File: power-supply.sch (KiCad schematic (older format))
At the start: 99 parts, among them IC1 TPS54561, J12 S2B-PH-K-S_LF__SN_, Q1 IRLML6402TRPBF, Q10 2N7002, Q11 2N7002, Q2 IRLML6402TRPBF, Q3 IRLML6402TRPBF, Q4 IRLML6402TRPBF, Q5 IRLML6402TRPBF, Q6 IRLML6402TRPBF, Q7 2N7002, Q8 2N7002, Q9 2N7002, U10 TPS62823DLCT, U11 TPS62823DLCT, U12 TPS62823DLCT, U13 TPS62823DLCT, U15 SN74LVC1G08DCKR, U16 SN74LS08DBR, U9 LM3881MME_NOPB

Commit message: Swapped PHY, P-MOSFETs fix
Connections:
- wire segments 349 -> 355
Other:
- moved on the sheet: C65, C66, C67, C68, C69, C70, C71, C72, C73, C74, D3, IC1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

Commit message: Cleaned up power sequencer
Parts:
- removed Q1, Q2, Q3, Q4, Q5, Q6: IRLML6402TRPBF, artix-dc-scm-footprints:SOT-23-3, symbol artix-dc-scm:IRLML6402TRPBF
- removed U15: SN74LVC1G08DCKR, artix-dc-scm-footprints:SC-70-5, symbol artix-dc-scm:SN74LVC1G08DCKR
- removed U16: SN74LS08DBR, artix-dc-scm-footprints:SOP65P775X265-14N, symbol artix-dc-scm:SN74LS08DBR
- added R138, R14, R15, R16: R_0R_0402, artix-dc-scm-footprints:0402-res, symbol artix-dc-scm:R_0R_0402
- added R139, R140, R141, R142: R_0R_1206, artix-dc-scm-footprints:1206-res, symbol artix-dc-scm:R_0R_1206
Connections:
- net labels removed: HPM_STBY_EN, HPM_STBY_RDY, ROT_RDY\ROT_GPIO0, VCC1V35_BANK, VCC1V35_DDR3, VCC1V8_BANK, VCC3V3_BANK, VCCAUX, VCCINT, VR1_PG, VR2_PG, VR_GOOD
- wire segments 355 -> 316
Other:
- note added: "STEP1: FPGA VCCINT (1V0)\nSTEP2: FPGA VCCAUX (1V8)\nSTEP3: FPGA VCCIO (3V3, 1V8), HPM reset is de-asserted\nSTEP4: HPM boots"
- note removed: "RoT booted flag pin"
- note removed: "STEP1: VRs start and RoT boots (HPM_STBY_EN when both are done)\nSTEP2: HPM starts its VRs and sets HPM_STBY_RDY when done\nSTEP3: FPGA VCCINT (1.0V)\nSTEP4: FPGA VCCAUX + DDR3 (1.8V, 1.35V)\nSTEP5: FPGA VCCIO + DDR3 (3.3V, DDRVTT), HPM reset is de-asserted\nSTEP6: HPM boots"
- note removed: "^ TODO: decide which DC-SCI pin connected\n to FPGA does this"
- moved on the sheet: C64, J12, R62, R63, R64, R65, U9

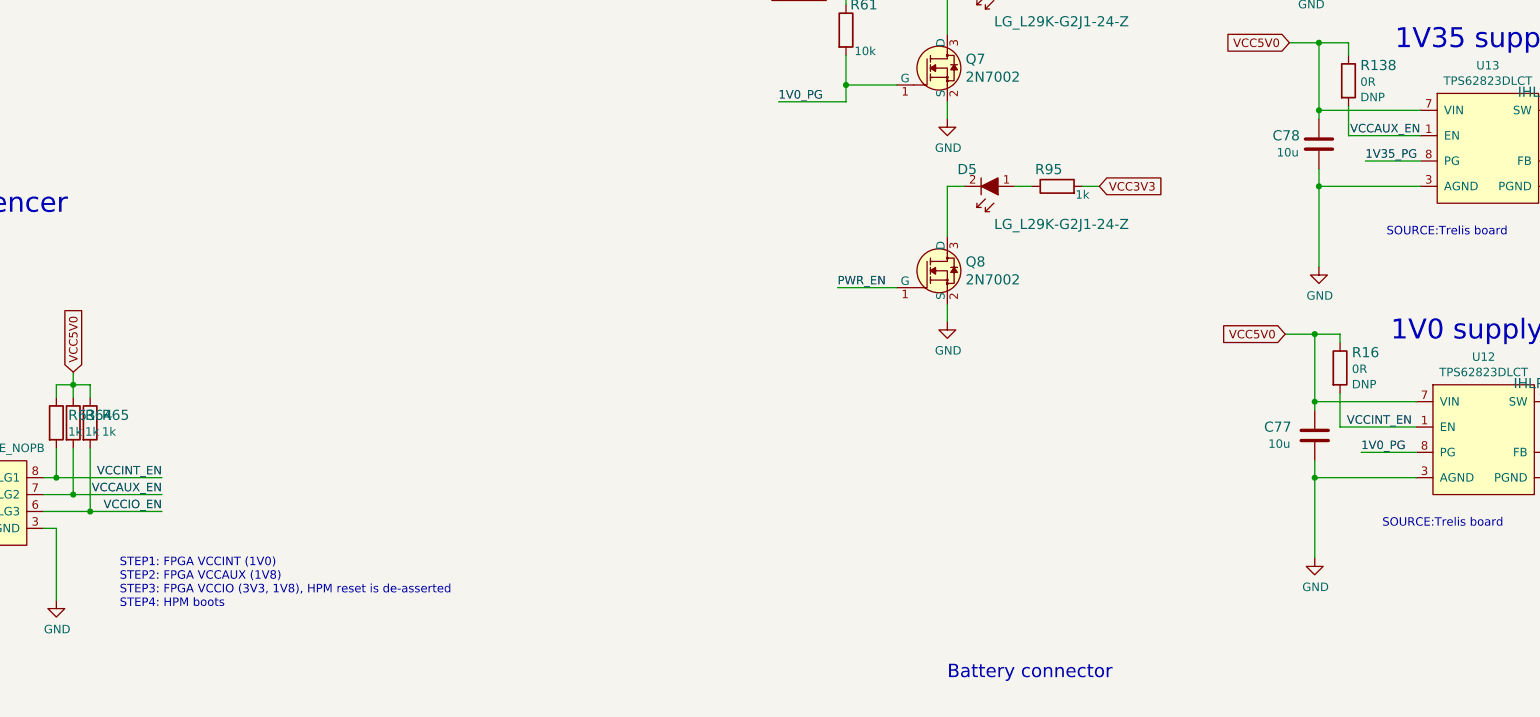
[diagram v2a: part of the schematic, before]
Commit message: Updated voltage supply labels, connected gpios left
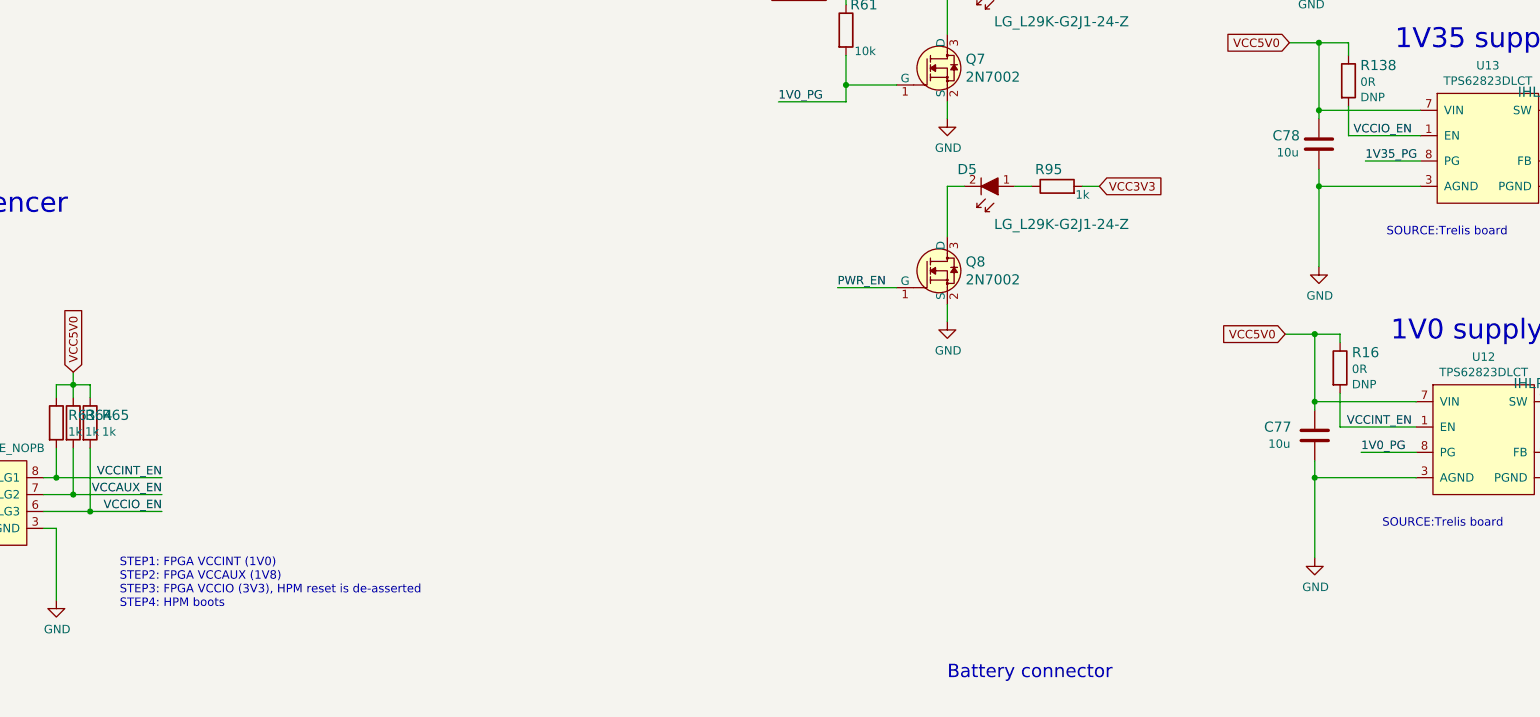
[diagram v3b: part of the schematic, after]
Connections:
- net VCCAUX_EN: no longer R138.2, U13.1 (EN)
- net VCCIO_EN: now also R138.2, U13.1 (EN)
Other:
- note added: "STEP1: FPGA VCCINT (1V0)\nSTEP2: FPGA VCCAUX (1V8)\nSTEP3: FPGA VCCIO (3V3), HPM reset is de-asserted\nSTEP4: HPM boots"
- note removed: "STEP1: FPGA VCCINT (1V0)\nSTEP2: FPGA VCCAUX (1V8)\nSTEP3: FPGA VCCIO (3V3, 1V8), HPM reset is de-asserted\nSTEP4: HPM boots"
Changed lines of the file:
@@
 VCC5V0
 Text Notes 5350 9675 0    50   ~ 0
-STEP1: FPGA VCCINT (1V0)\nSTEP2: FPGA VCCAUX (1V8)\nSTEP3: FPGA VCCIO (3V3, 1V8), HPM reset is de-asserted\nSTEP4: HPM boots
+STEP1: FPGA VCCINT (1V0)\nSTEP2: FPGA VCCAUX (1V8)\nSTEP3: FPGA VCCIO (3V3), HPM reset is de-asserted\nSTEP4: HPM boots
 Wire Wire Line
 	12375 2750 12975 2750
@@
 Wire Wire Line
 	12575 8600 13025 8600
-Text Label 13050 6875 2    50   ~ 0
-VCCAUX_EN
 Text Label 13000 5050 2    50   ~ 0
 VCCAUX_EN
@@
 	0    1    1    0
 $EndComp
+Text Label 13000 6875 2    50   ~ 0
+VCCIO_EN
 $EndSCHEMATC

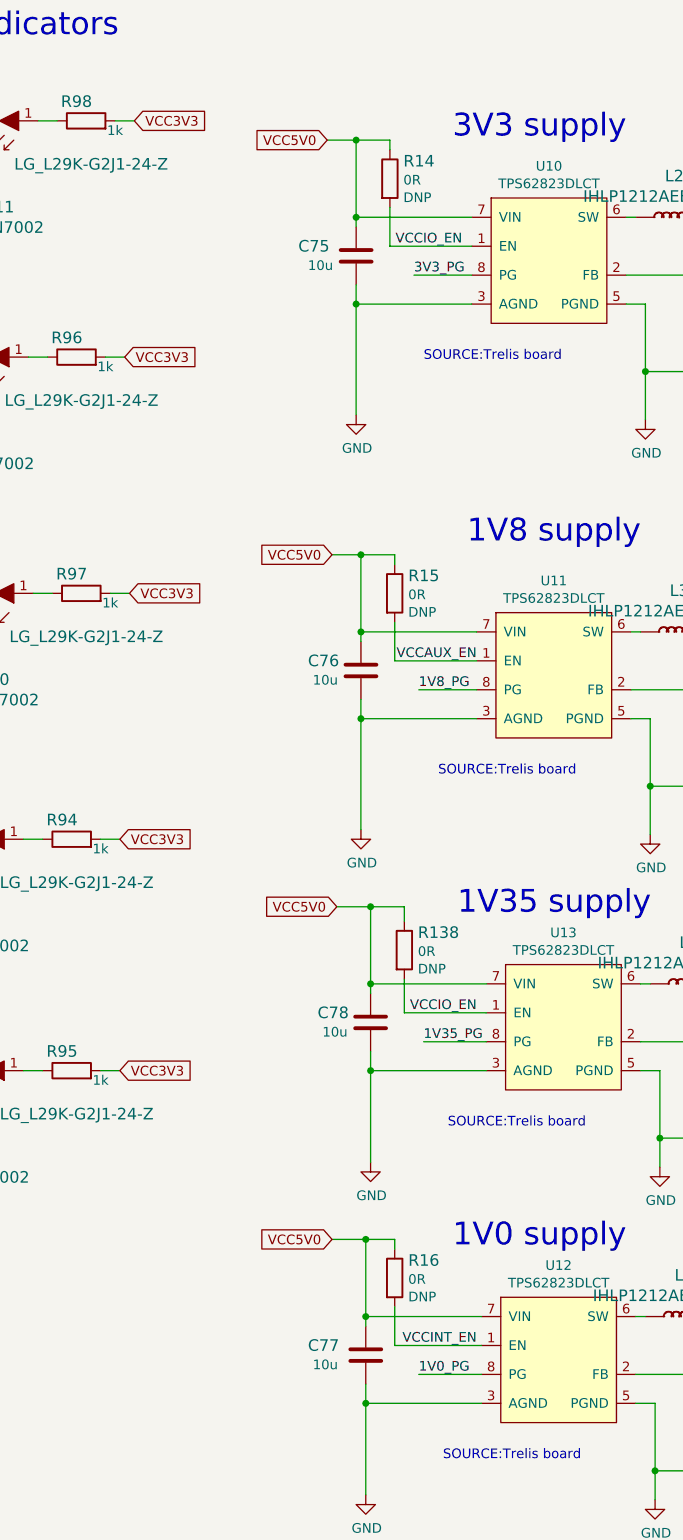
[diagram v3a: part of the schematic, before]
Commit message: Fixed EN signals 0Rs
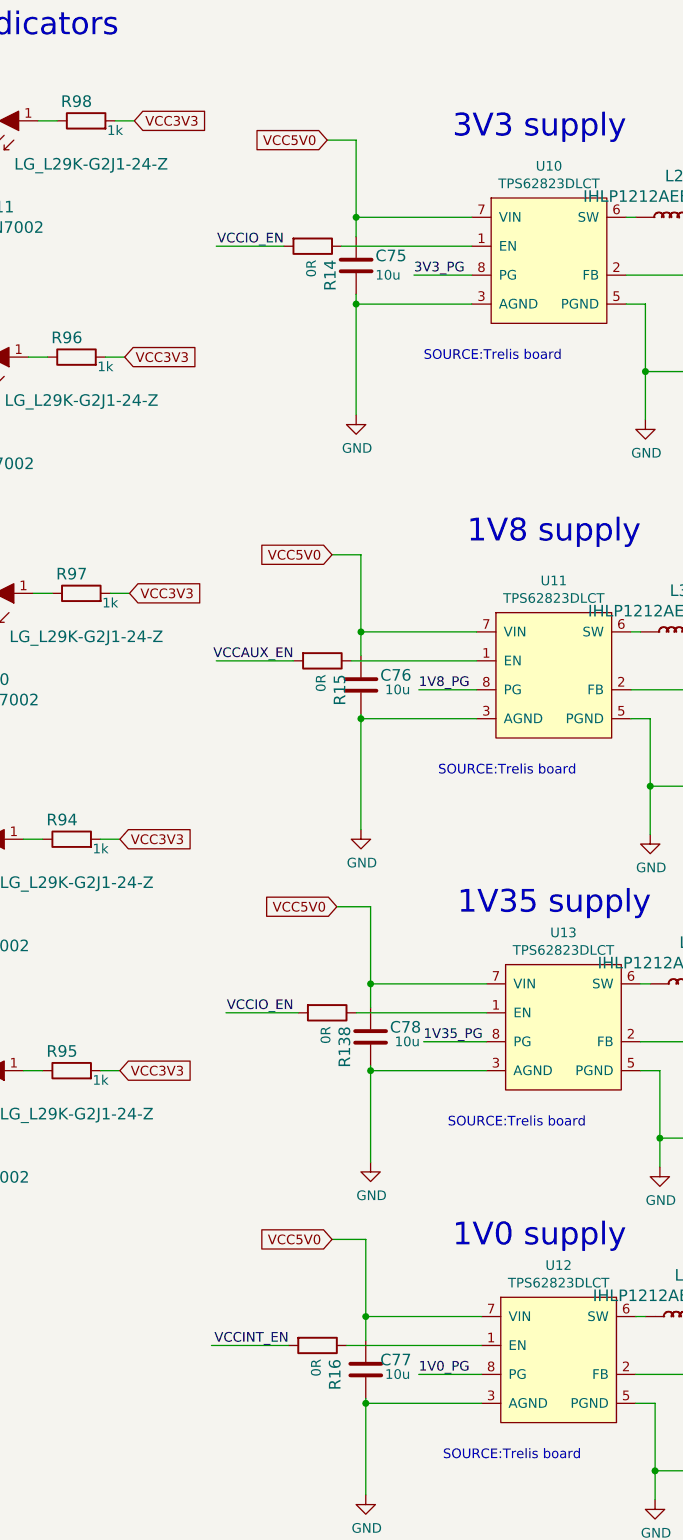
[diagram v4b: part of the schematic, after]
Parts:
- R138, R14, R15, R16: Populate DNP -> (none)
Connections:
- net VCC5V0: no longer R138.1, R14.1, R15.1, R16.1
- net VCCAUX_EN: no longer U11.1 (EN)
- net VCCINT_EN: no longer U12.1 (EN)
- net VCCIO_EN: no longer U10.1 (EN), U13.1 (EN)
- new net: R14.1, U10.1 (EN)
- new net: R15.1, U11.1 (EN)
- new net: R138.1, U13.1 (EN)
- new net: R16.1, U12.1 (EN)
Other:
- moved on the sheet: C75, C76, C77, C78, R138, R14, R15, R16

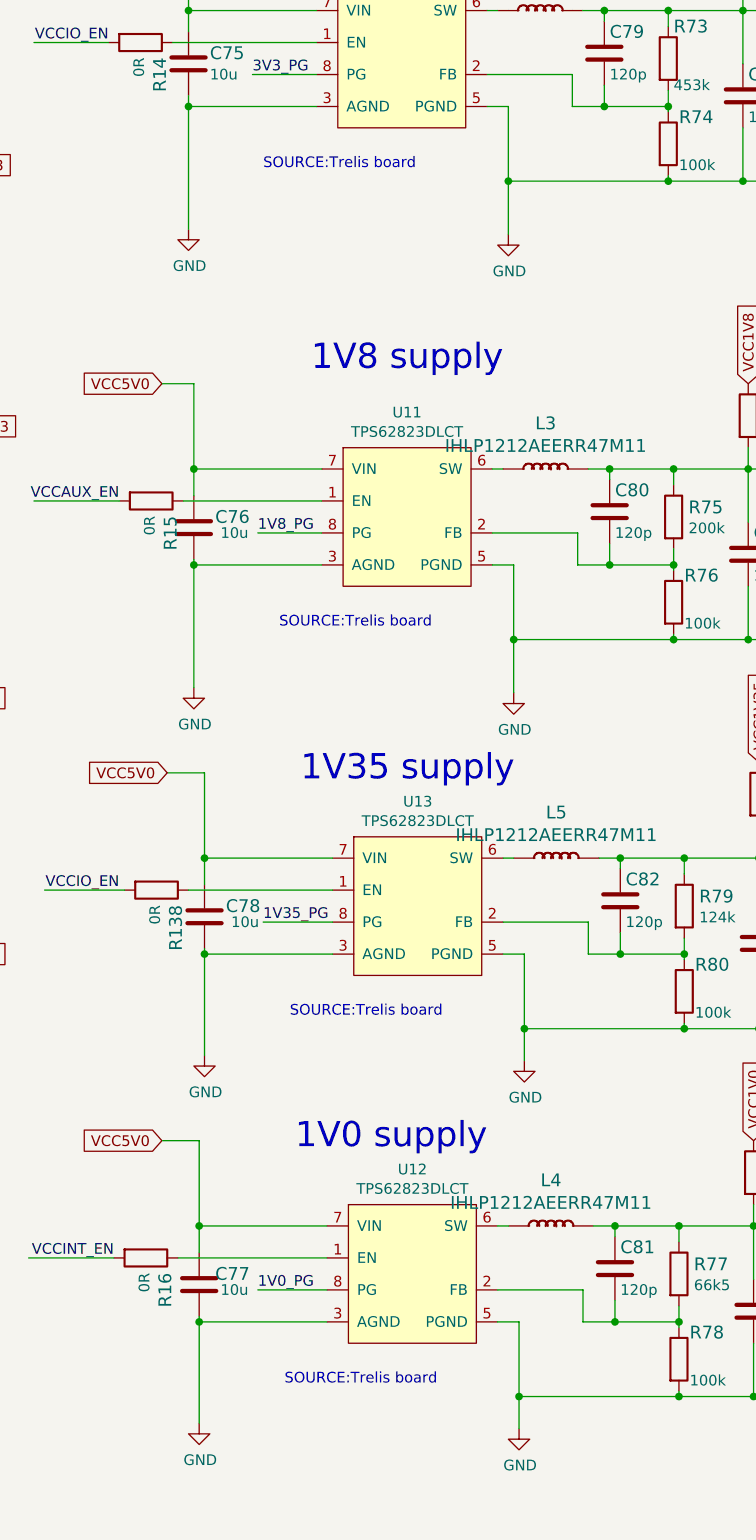
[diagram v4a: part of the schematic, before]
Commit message: Update layout around filtering caps
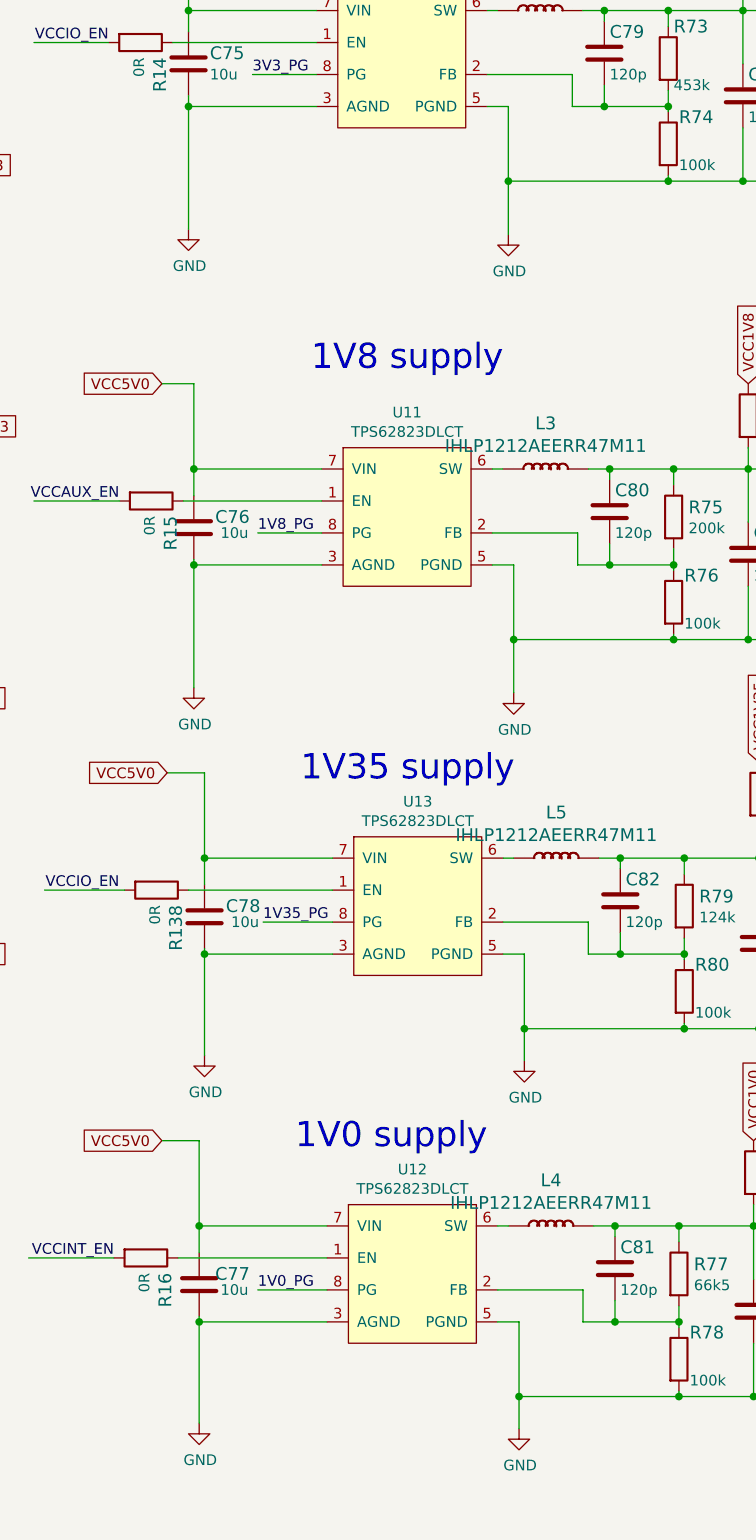
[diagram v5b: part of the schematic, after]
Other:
- note removed: "SOURCE:Trelis board"
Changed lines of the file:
@@
 Wire Wire Line
 	14975 2650 14975 2750
-Text Notes 12725 3500 0    50   ~ 0
-SOURCE:Trelis board
 Wire Wire Line
 	12675 3050 12975 3050
@@
 Wire Wire Line
 	15000 4800 15000 4900
-Text Notes 12800 5650 0    50   ~ 0
-SOURCE:Trelis board
 Wire Wire Line
 	12700 5200 13000 5200
@@
 Wire Wire Line
 	15050 6575 15050 6725
-Text Notes 12850 7475 0    50   ~ 0
-SOURCE:Trelis board
 Wire Wire Line
 	12725 7025 13050 7025
@@
 Wire Wire Line
 	15025 8350 15025 8450
-Text Notes 12825 9200 0    50   ~ 0
-SOURCE:Trelis board
 Wire Wire Line
 	12700 8750 13025 8750
